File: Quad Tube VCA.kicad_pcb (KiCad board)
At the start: 2 copper layers, 162.6 x 100.3 mm, 226 parts, among them IC1 TL072, IC10 TL072, IC2 LM358, IC3 TL072, IC4 LM358, IC5 TL072, IC6 LM358, IC7 TL072, IC8 LM358, IC9 TL072

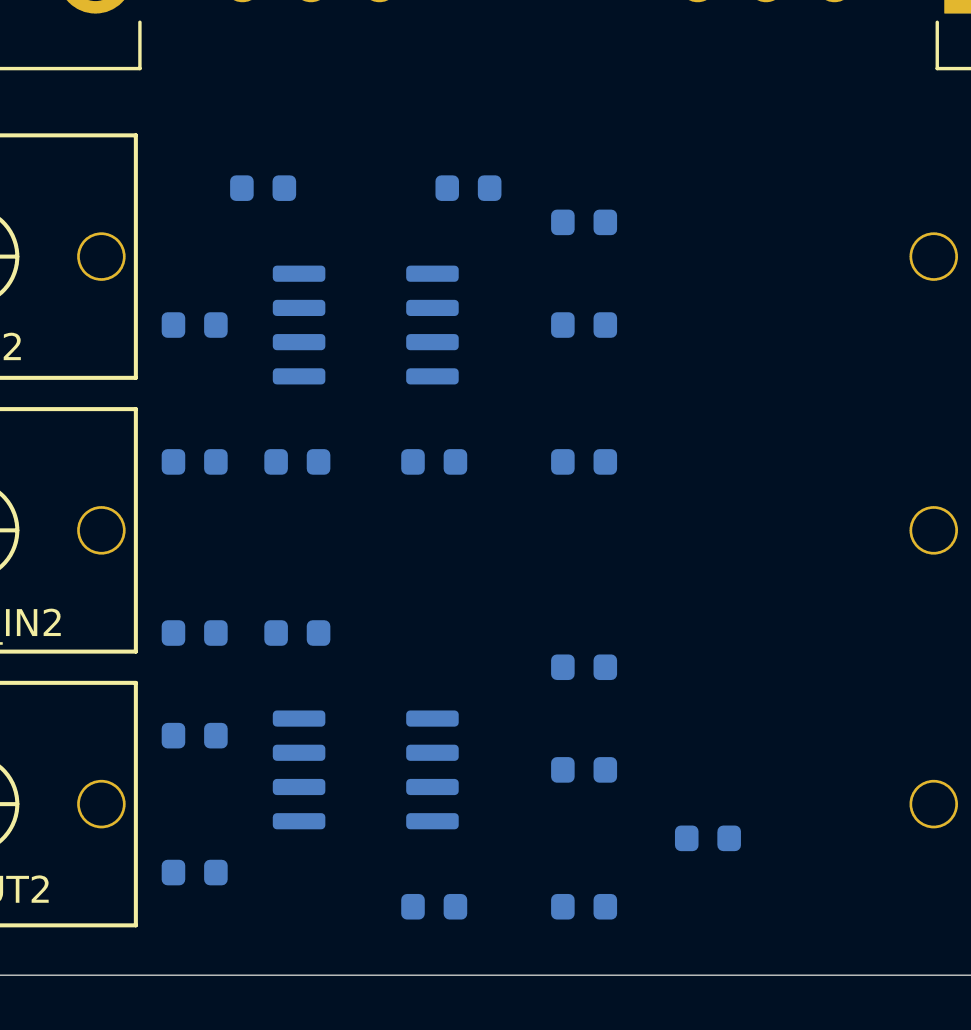
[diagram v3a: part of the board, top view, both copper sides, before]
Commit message: syncs pcb/schem
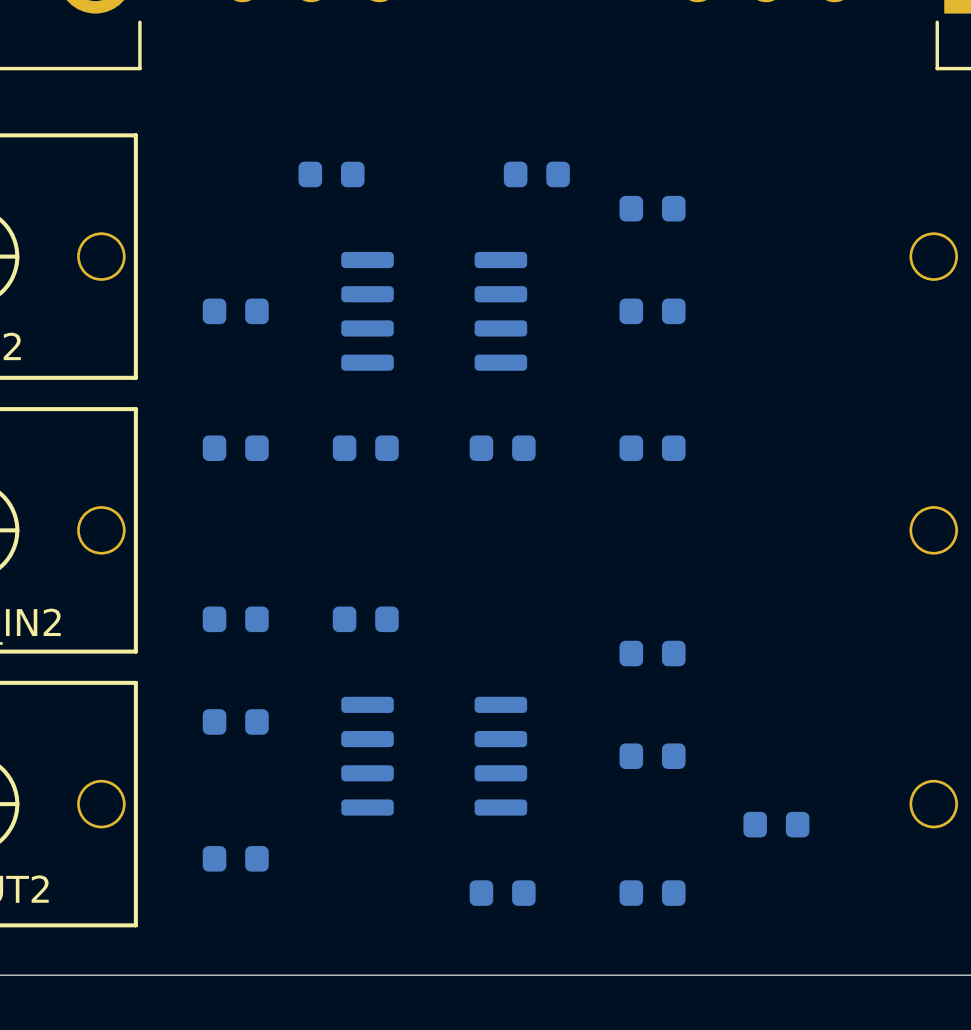
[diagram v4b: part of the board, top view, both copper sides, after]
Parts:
- moved C20 2.59 mm to (151.6, 120.1)
- moved C22 2.59 mm to (146.1, 141.7)
- moved C23 2.59 mm to (146.1, 125.2)
- moved R22 2.59 mm to (151.6, 136.7)
- moved R23 2.59 mm to (151.6, 141.7)
- moved R35 2.59 mm to (151.6, 125.2)
- moved R40 2.59 mm to (151.6, 116.3)
- moved C16 2.59 mm to (156.2, 139.2)
- moved R21 2.59 mm to (151.6, 132.8)
- moved C24 2.59 mm to (141.0, 131.6)
- moved IC3 2.59 mm to (143.5, 136.7)
- moved IC4 2.59 mm to (143.5, 120.1)
- moved R36 2.59 mm to (141.0, 125.2)
- moved C25 2.59 mm to (139.7, 115.1)
- moved C26 2.59 mm to (147.3, 115.1)
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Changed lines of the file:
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@@
   )
   (module Resistor_SMD:R_0603_1608Metric (layer B.Cu)
-    (at 149.0725 116.84)
+    (at 151.6125 116.332)
     (descr "Resistor SMD 0603 (1608 Metric), square (rectangular) end terminal, IPC_7351 nominal, (Body size source: http://www.tortai-tech.com/upload/download/2011102023233369053.pdf), generated with kicad-footprint-generator")
     (tags resistor)
@@
   )
   (module Resistor_SMD:R_0603_1608Metric (layer B.Cu)
-    (at 134.62 125.73)
+    (at 136.144 125.222)
     (descr "Resistor SMD 0603 (1608 Metric), square (rectangular) end terminal, IPC_7351 nominal, (Body size source: http://www.tortai-tech.com/upload/download/2011102023233369053.pdf), generated with kicad-footprint-generator")
     (tags resistor)
@@
   )
   (module Resistor_SMD:R_0603_1608Metric (layer B.Cu)
-    (at 138.43 125.73)
+    (at 140.97 125.222)
     (descr "Resistor SMD 0603 (1608 Metric), square (rectangular) end terminal, IPC_7351 nominal, (Body size source: http://www.tortai-tech.com/upload/download/2011102023233369053.pdf), generated with kicad-footprint-generator")
     (tags resistor)
@@
   )
   (module Resistor_SMD:R_0603_1608Metric (layer B.Cu)
-    (at 149.0725 125.73)
+    (at 151.6125 125.222)
     (descr "Resistor SMD 0603 (1608 Metric), square (rectangular) end terminal, IPC_7351 nominal, (Body size source: http://www.tortai-tech.com/upload/download/2011102023233369053.pdf), generated with kicad-footprint-generator")
     (tags resistor)
@@
   )
   (module Resistor_SMD:R_0603_1608Metric (layer B.Cu)
-    (at 134.62 140.97 180)
+    (at 136.144 140.462 180)
     (descr "Resistor SMD 0603 (1608 Metric), square (rectangular) end terminal, IPC_7351 nominal, (Body size source: http://www.tortai-tech.com/upload/download/2011102023233369053.pdf), generated with kicad-footprint-generator")
     (tags resistor)
@@
   )
   (module Resistor_SMD:R_0603_1608Metric (layer B.Cu)
-    (at 134.62 132.08)
+    (at 136.144 131.572)
     (descr "Resistor SMD 0603 (1608 Metric), square (rectangular) end terminal, IPC_7351 nominal, (Body size source: http://www.tortai-tech.com/upload/download/2011102023233369053.pdf), generated with kicad-footprint-generator")
     (tags resistor)
@@
   )
   (module Resistor_SMD:R_0603_1608Metric (layer B.Cu)
-    (at 149.0725 142.24 180)
+    (at 151.6125 141.732 180)
     (descr "Resistor SMD 0603 (1608 Metric), square (rectangular) end terminal, IPC_7351 nominal, (Body size source: http://www.tortai-tech.com/upload/download/2011102023233369053.pdf), generated with kicad-footprint-generator")
     (tags resistor)
@@
   )
   (module Resistor_SMD:R_0603_1608Metric (layer B.Cu)
-    (at 149.0725 137.16)
+    (at 151.6125 136.652)
     (descr "Resistor SMD 0603 (1608 Metric), square (rectangular) end terminal, IPC_7351 nominal, (Body size source: http://www.tortai-tech.com/upload/download/2011102023233369053.pdf), generated with kicad-footprint-generator")
     (tags resistor)
@@
   )
   (module Resistor_SMD:R_0603_1608Metric (layer B.Cu)
-    (at 149.0725 133.35)
+    (at 151.6125 132.842)
     (descr "Resistor SMD 0603 (1608 Metric), square (rectangular) end terminal, IPC_7351 nominal, (Body size source: http://www.tortai-tech.com/upload/download/2011102023233369053.pdf), generated with kicad-footprint-generator")
     (tags resistor)
@@
   )
   (module Package_SO:SOIC-8_3.9x4.9mm_P1.27mm (layer B.Cu)
-    (at 140.97 120.65)
+    (at 143.51 120.142)
     (descr "SOIC, 8 Pin (JEDEC MS-012AA, https://www.analog.com/media/en/package-pcb-resources/package/pkg_pdf/soic_narrow-r/r_8.pdf), generated with kicad-footprint-generator ipc_gullwing_generator.py")
     (tags "SOIC SO")
@@
   )
   (module Package_SO:SOIC-8_3.9x4.9mm_P1.27mm (layer B.Cu)
-    (at 140.97 137.16)
+    (at 143.51 136.652)
     (descr "SOIC, 8 Pin (JEDEC MS-012AA, https://www.analog.com/media/en/package-pcb-resources/package/pkg_pdf/soic_narrow-r/r_8.pdf), generated with kicad-footprint-generator ipc_gullwing_generator.py")
     (tags "SOIC SO")
@@
   )
   (module Capacitor_SMD:C_0603_1608Metric (layer B.Cu)
-    (at 144.78 115.57)
+    (at 147.32 115.062)
     (descr "Capacitor SMD 0603 (1608 Metric), square (rectangular) end terminal, IPC_7351 nominal, (Body size source: http://www.tortai-tech.com/upload/download/2011102023233369053.pdf), generated with kicad-footprint-generator")
     (tags capacitor)
@@
   )
   (module Capacitor_SMD:C_0603_1608Metric (layer B.Cu)
-    (at 137.16 115.57)
+    (at 139.7 115.062)
     (descr "Capacitor SMD 0603 (1608 Metric), square (rectangular) end terminal, IPC_7351 nominal, (Body size source: http://www.tortai-tech.com/upload/download/2011102023233369053.pdf), generated with kicad-footprint-generator")
     (tags capacitor)
@@
   )
   (module Capacitor_SMD:C_0603_1608Metric (layer B.Cu)
-    (at 138.43 132.08)
+    (at 140.97 131.572)
     (descr "Capacitor SMD 0603 (1608 Metric), square (rectangular) end terminal, IPC_7351 nominal, (Body size source: http://www.tortai-tech.com/upload/download/2011102023233369053.pdf), generated with kicad-footprint-generator")
     (tags capacitor)
@@
   )
   (module Capacitor_SMD:C_0603_1608Metric (layer B.Cu)
-    (at 143.51 125.73)
+    (at 146.05 125.222)
     (descr "Capacitor SMD 0603 (1608 Metric), square (rectangular) end terminal, IPC_7351 nominal, (Body size source: http://www.tortai-tech.com/upload/download/2011102023233369053.pdf), generated with kicad-footprint-generator")
     (tags capacitor)
@@
   )
   (module Capacitor_SMD:C_0603_1608Metric (layer B.Cu)
-    (at 143.51 142.24)
+    (at 146.05 141.732)
     (descr "Capacitor SMD 0603 (1608 Metric), square (rectangular) end terminal, IPC_7351 nominal, (Body size source: http://www.tortai-tech.com/upload/download/2011102023233369053.pdf), generated with kicad-footprint-generator")
     (tags capacitor)
@@
   )
   (module Capacitor_SMD:C_0603_1608Metric (layer B.Cu)
-    (at 134.62 120.65)
+    (at 136.144 120.142)
     (descr "Capacitor SMD 0603 (1608 Metric), square (rectangular) end terminal, IPC_7351 nominal, (Body size source: http://www.tortai-tech.com/upload/download/2011102023233369053.pdf), generated with kicad-footprint-generator")
     (tags capacitor)
@@
   )
   (module Capacitor_SMD:C_0603_1608Metric (layer B.Cu)
-    (at 149.0725 120.65)
+    (at 151.6125 120.142)
     (descr "Capacitor SMD 0603 (1608 Metric), square (rectangular) end terminal, IPC_7351 nominal, (Body size source: http://www.tortai-tech.com/upload/download/2011102023233369053.pdf), generated with kicad-footprint-generator")
     (tags capacitor)
@@
   )
   (module Capacitor_SMD:C_0603_1608Metric (layer B.Cu)
-    (at 153.67 139.7)
+    (at 156.21 139.192)
     (descr "Capacitor SMD 0603 (1608 Metric), square (rectangular) end terminal, IPC_7351 nominal, (Body size source: http://www.tortai-tech.com/upload/download/2011102023233369053.pdf), generated with kicad-footprint-generator")
     (tags capacitor)
@@
   )
   (module Capacitor_SMD:C_0603_1608Metric (layer B.Cu)
-    (at 134.62 135.89)
+    (at 136.144 135.382)
     (descr "Capacitor SMD 0603 (1608 Metric), square (rectangular) end terminal, IPC_7351 nominal, (Body size source: http://www.tortai-tech.com/upload/download/2011102023233369053.pdf), generated with kicad-footprint-generator")
     (tags capacitor)

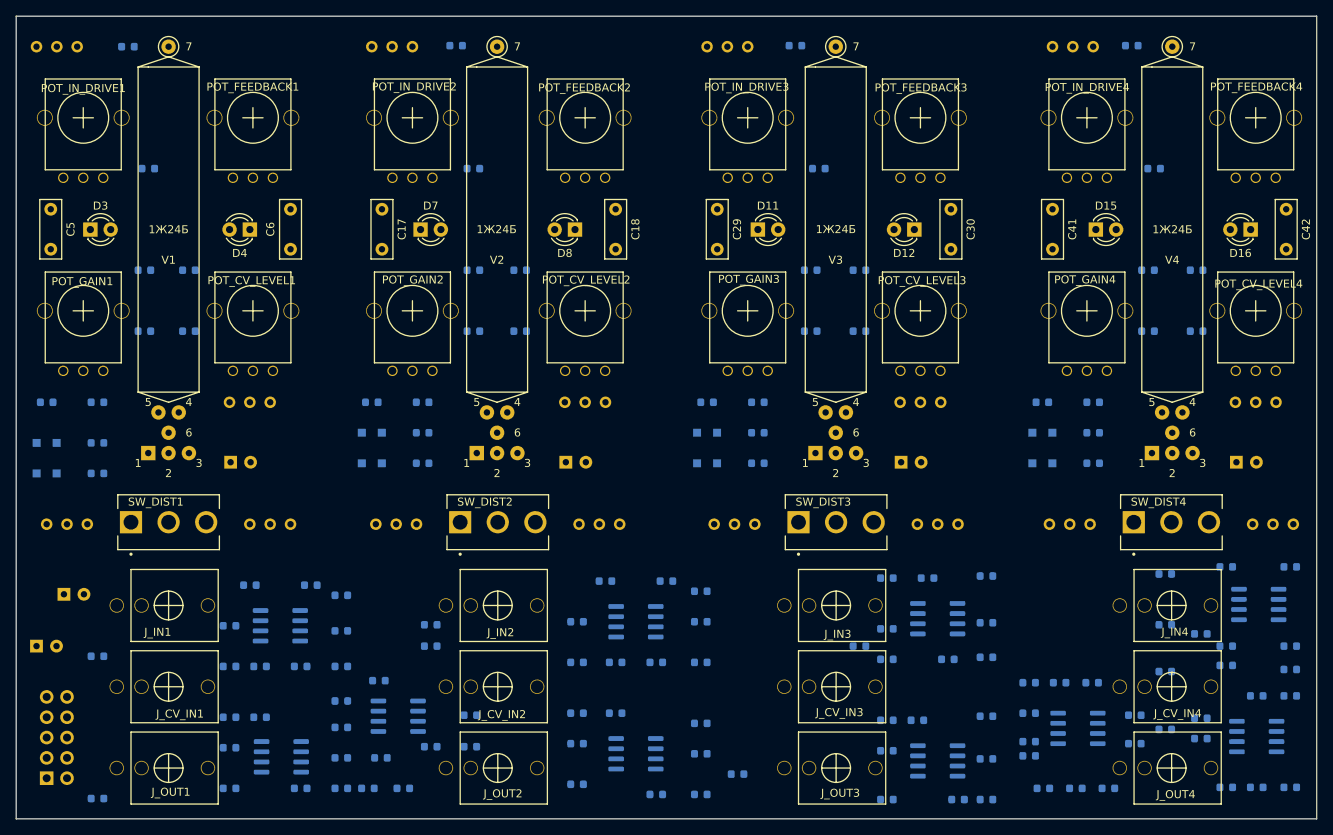
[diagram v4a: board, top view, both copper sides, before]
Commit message: first GND pour
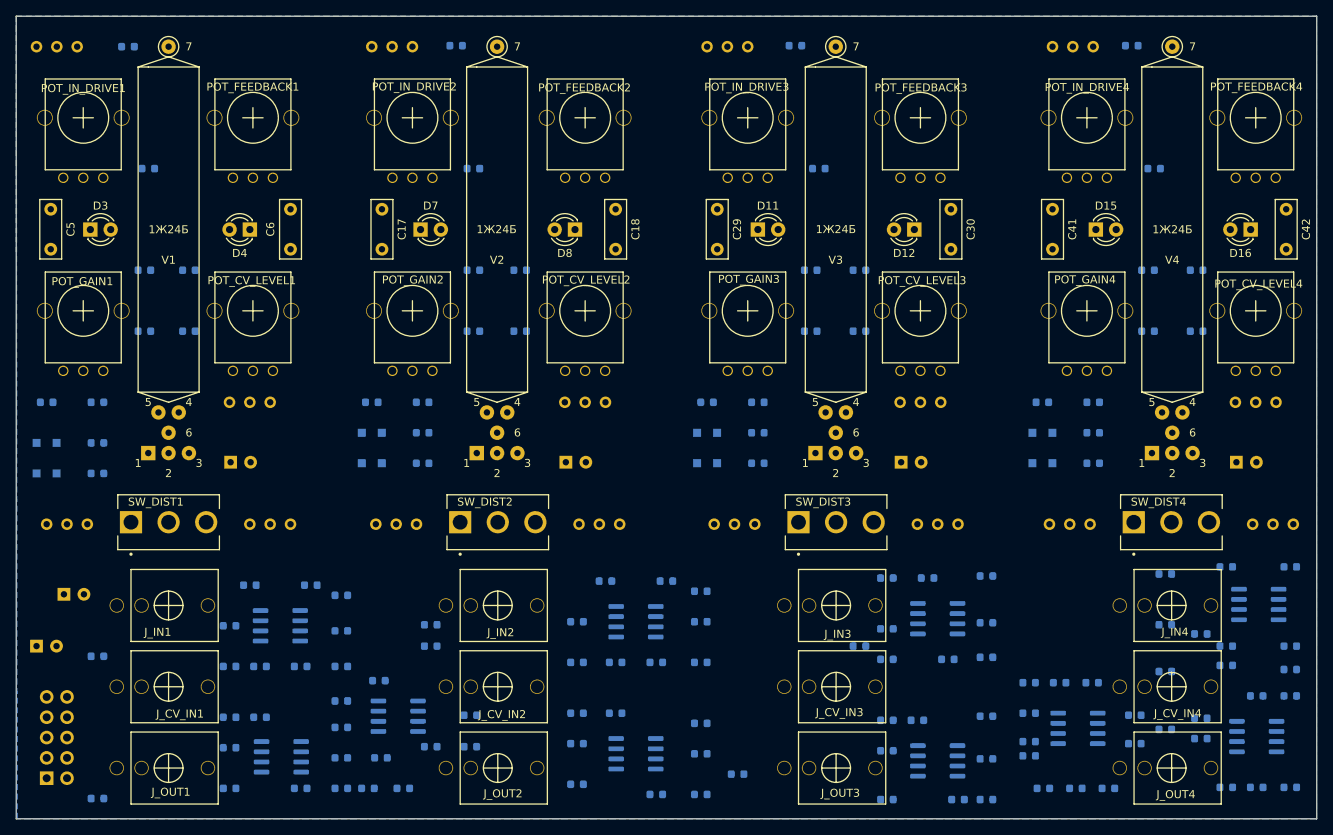
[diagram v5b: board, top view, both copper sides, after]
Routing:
- added copper zone on B.Cu, net GND
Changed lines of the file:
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@@
+    )
+  )
+  (zone (net 3) (net_name GND) (layer B.Cu) (hatch edge 0.508)
+    (connect_pads (clearance 0.508))
+    (min_thickness 0.254)
+    (fill yes (arc_segments 32) (thermal_gap 0.508) (thermal_bridge_width 0.508))
+    (polygon
+      (pts
+        (xy 228.6 144.78) (xy 66.167 144.78) (xy 66.04 44.577) (xy 66.04 44.45) (xy 228.6 44.45)
+      )
     )
   )
